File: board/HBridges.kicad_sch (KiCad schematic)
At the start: 66 parts, among them Q1 NMOS, Q2 NMOS, Q3 NMOS, Q4 NMOS, Q7 NMOS, Q8 NMOS

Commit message: Adjusted diode footprints and grouped layout components
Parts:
- C2, C24, C8: footprint BoCoFootprintLibrary:U1-Z_NCH -> Capacitor_THT:CP_Radial_D12.5mm_P5.00mm
- CR1, CR2, CR3, CR4, CR7, CR8: footprint BoCoFootprintLibrary:DO-35_STM -> Diode_THT:D_DO-35_SOD27_P3.81mm_Vertical_KathodeUp
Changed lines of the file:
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@@
 			)
 		)
-		(property "Footprint" "BoCoFootprintLibrary:U1-Z_NCH"
+		(property "Footprint" "Capacitor_THT:CP_Radial_D12.5mm_P5.00mm"
 			(at 128.27 31.75 0)
 			(effects
@@
 			)
 		)
-		(property "Footprint" "BoCoFootprintLibrary:DO-35_STM"
+		(property "Footprint" "Diode_THT:D_DO-35_SOD27_P3.81mm_Vertical_KathodeUp"
 			(at 158.75 86.36 0)
 			(effects
@@
 			)
 		)
-		(property "Footprint" "BoCoFootprintLibrary:DO-35_STM"
+		(property "Footprint" "Diode_THT:D_DO-35_SOD27_P3.81mm_Vertical_KathodeUp"
 			(at 158.75 41.91 0)
 			(effects
@@
 			)
 		)
-		(property "Footprint" "BoCoFootprintLibrary:DO-35_STM"
+		(property "Footprint" "Diode_THT:D_DO-35_SOD27_P3.81mm_Vertical_KathodeUp"
 			(at 93.98 86.36 0)
 			(effects
@@
 			)
 		)
-		(property "Footprint" "BoCoFootprintLibrary:U1-Z_NCH"
+		(property "Footprint" "Capacitor_THT:CP_Radial_D12.5mm_P5.00mm"
 			(at 63.5 31.75 0)
 			(effects
@@
 			)
 		)
-		(property "Footprint" "BoCoFootprintLibrary:DO-35_STM"
+		(property "Footprint" "Diode_THT:D_DO-35_SOD27_P3.81mm_Vertical_KathodeUp"
 			(at 93.98 41.91 0)
 			(effects
@@
 			)
 		)
-		(property "Footprint" "BoCoFootprintLibrary:DO-35_STM"
+		(property "Footprint" "Diode_THT:D_DO-35_SOD27_P3.81mm_Vertical_KathodeUp"
 			(at 29.21 41.91 0)
 			(effects
@@
 			)
 		)
-		(property "Footprint" "BoCoFootprintLibrary:DO-35_STM"
+		(property "Footprint" "Diode_THT:D_DO-35_SOD27_P3.81mm_Vertical_KathodeUp"
 			(at 29.21 86.36 0)
 			(effects
@@
 			)
 		)
-		(property "Footprint" "BoCoFootprintLibrary:U1-Z_NCH"
+		(property "Footprint" "Capacitor_THT:CP_Radial_D12.5mm_P5.00mm"
 			(at 193.04 31.75 0)
 			(effects

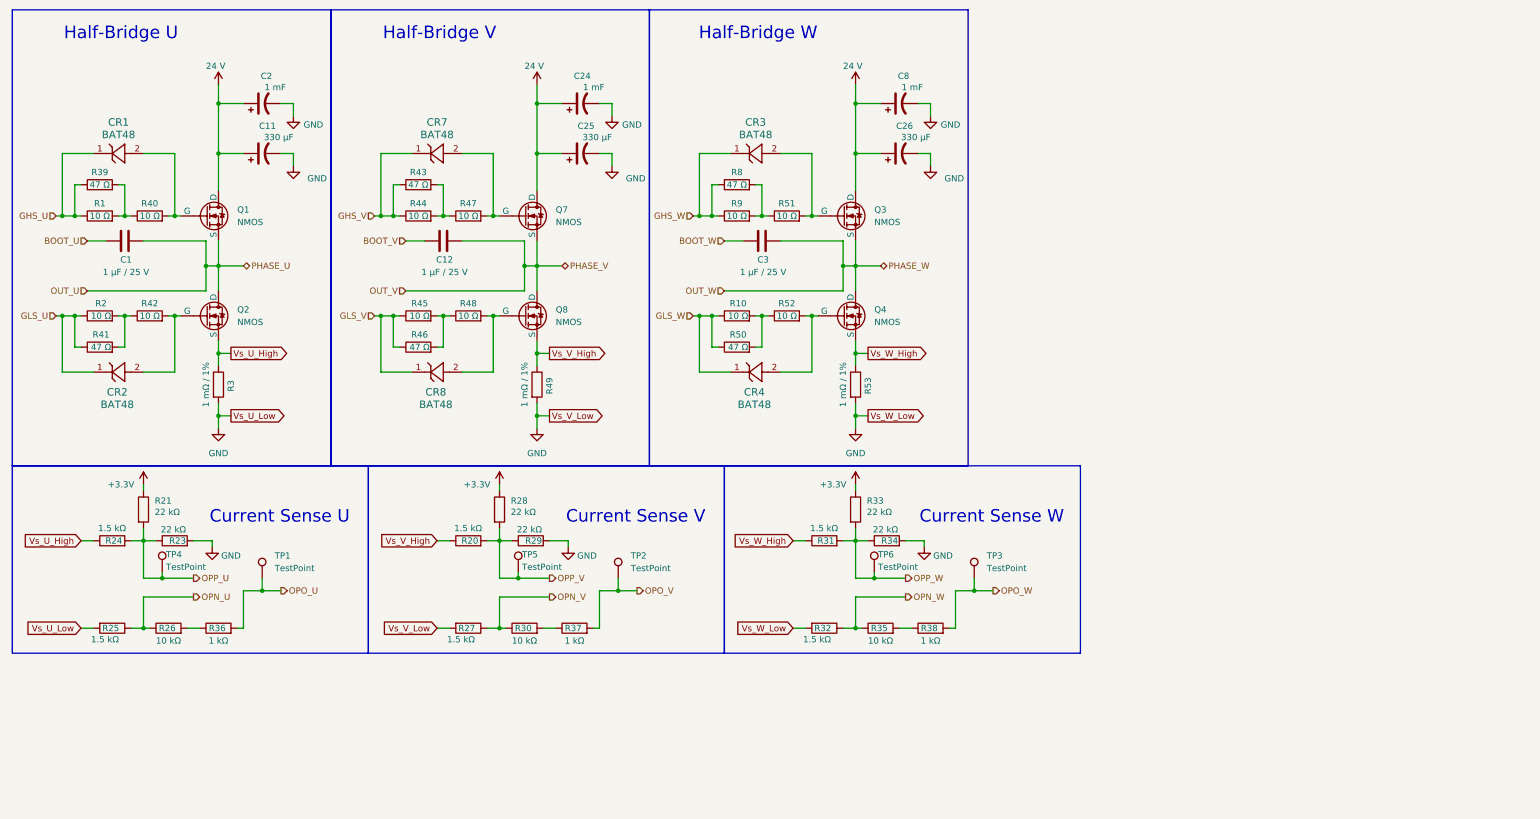
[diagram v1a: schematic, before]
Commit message: Placed some basic planes in the layout and swapped mosfet symbols to match layout footprints.
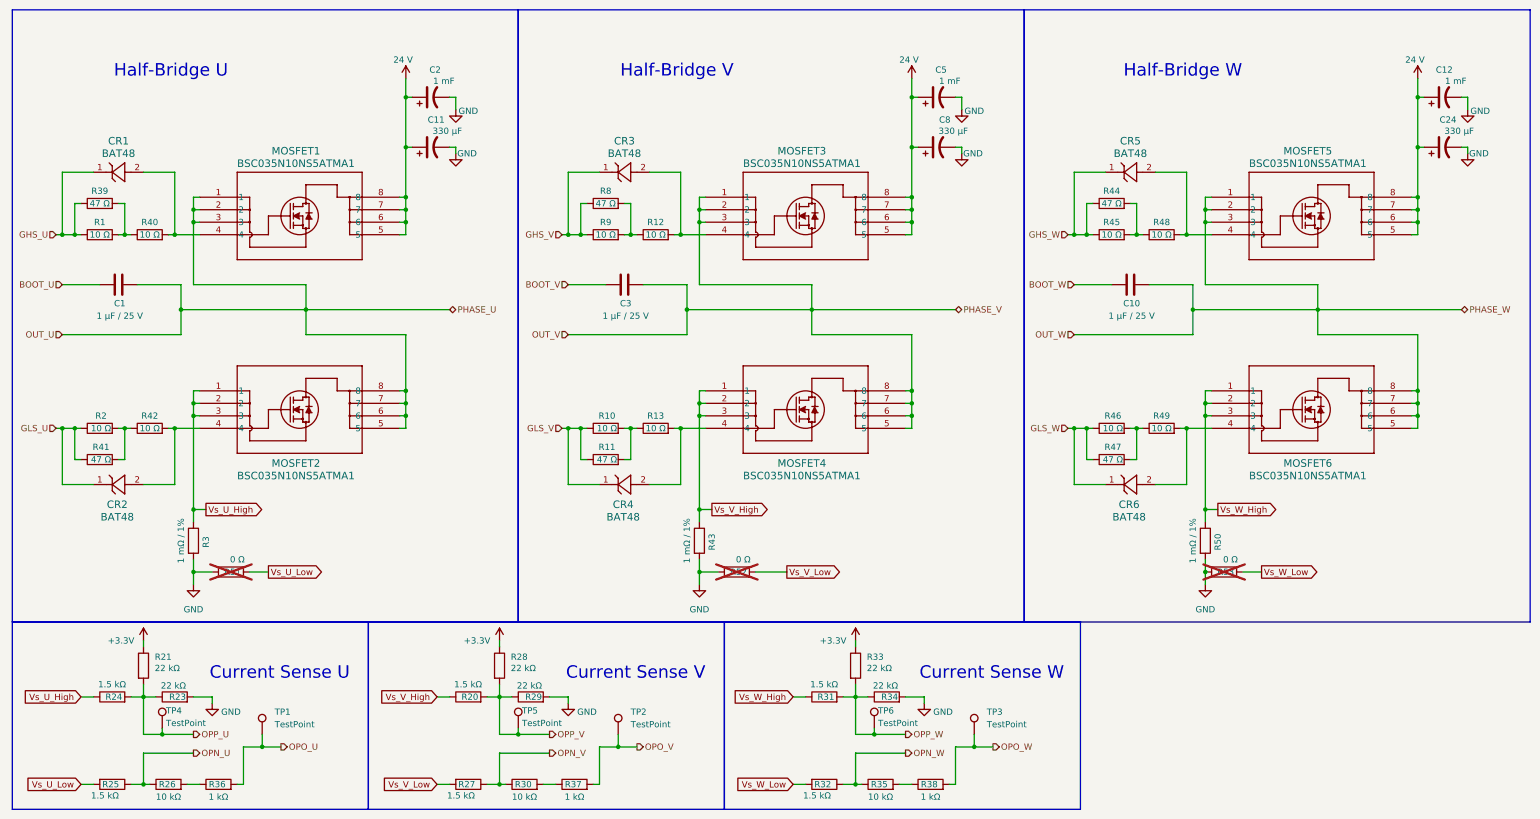
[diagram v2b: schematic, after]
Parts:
- removed C12: 1 µF / 25 V, Capacitor_SMD:C_0603_1608Metric_Pad1.08x0.95mm_HandSolder, symbol Device:C
- removed C25, C26: 330 μF, BoCoFootprintLibrary:CAP_PAN_EEE_H13_PAN, symbol Device:C_Polarized_US
- removed CR7, CR8: BAT48, Diode_THT:D_DO-35_SOD27_P3.81mm_Vertical_KathodeUp, symbol BAT48:BAT48
- removed Q1, Q2, Q3, Q4, Q7, Q8: NMOS, BoCoFootprintLibrary:PG-TDSON-8_INF, symbol Simulation_SPICE:NMOS
- added C10: 1 µF / 25 V, Capacitor_SMD:C_0603_1608Metric_Pad1.08x0.95mm_HandSolder, symbol Device:C
- added C12, C5: 1 mF, Capacitor_THT:CP_Radial_D12.5mm_P5.00mm, symbol Device:C_Polarized_US
- added CR5, CR6: BAT48, Diode_THT:D_DO-35_SOD27_P3.81mm_Vertical_KathodeUp, symbol BAT48:BAT48
- added MOSFET1, MOSFET2, MOSFET3, MOSFET4, MOSFET5, MOSFET6: BSC035N10NS5ATMA1, PG-TDSON-8_INF, symbol BoCoSymbolLibrary:BSC035N10NS5ATMA1
- added R11: 47 Ω, Resistor_SMD:R_0603_1608Metric_Pad0.98x0.95mm_HandSolder, symbol Device:R
- added R12, R13: 10 Ω, Resistor_SMD:R_0603_1608Metric_Pad0.98x0.95mm_HandSolder, symbol Device:R
- C24, C8: value 1 mF -> 330 μF; footprint Capacitor_THT:CP_Radial_D12.5mm_P5.00mm -> BoCoFootprintLibrary:CAP_PAN_EEE_H13_PAN
- R43, R50: value 47 Ω -> 1 mΩ / 1%
- R44, R47: value 10 Ω -> 47 Ω
- R46: value 47 Ω -> 10 Ω
- R49: value 1 mΩ / 1% -> 10 Ω
- R51, R52: value 10 Ω -> 0 Ω; now not fitted
- R53: value 1 mΩ / 1% -> 0 Ω; now not fitted
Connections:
- net 24 V: now also C12.1, C5.1, MOSFET1.5, MOSFET1.6, MOSFET1.7, MOSFET1.8, MOSFET3.5, MOSFET3.6, MOSFET3.7, MOSFET3.8, MOSFET5.5, MOSFET5.6, MOSFET5.7, MOSFET5.8
- net BOOT_V: now also C3.1
- net BOOT_W: now also C10.1; no longer C3.1
- net GHS_V: now also CR3.1, R8.1, R9.1; no longer R43.1, R44.1
- net GHS_W: now also R44.1, R45.1, CR5.1; no longer CR3.1, R8.1, R9.1
- net GLS_V: now also CR4.1, R10.1, R11.1; no longer R45.1, R46.1
- net GLS_W: now also R46.1, R47.1, CR6.1; no longer CR4.1, R10.1, R50.1
- net GND: now also R43.2, R50.2, R51.1, R52.1, R53.1, C12.2, C5.2; no longer R25.2, R27.2, R32.2, R49.2, R53.2
- net OUT_U: now also MOSFET1.1, MOSFET1.2, MOSFET1.3, MOSFET2.5, MOSFET2.6, MOSFET2.7, MOSFET2.8
- net OUT_V: now also C3.2, MOSFET3.1, MOSFET3.2, MOSFET3.3, MOSFET4.5, MOSFET4.6, MOSFET4.7, MOSFET4.8
- net OUT_W: now also C10.2, MOSFET5.1, MOSFET5.2, MOSFET5.3, MOSFET6.5, MOSFET6.6, MOSFET6.7, MOSFET6.8; no longer C3.2
- net Vs_U_High: now also MOSFET2.1, MOSFET2.2, MOSFET2.3
- net Vs_V_High: now also R43.1, MOSFET4.1, MOSFET4.2, MOSFET4.3; no longer R49.1
- net Vs_W_High: now also R50.1, MOSFET6.1, MOSFET6.2, MOSFET6.3; no longer R53.1
- net at CR3.2: now also MOSFET3.4, R12.2; no longer R51.2
- net at CR4.2: now also MOSFET4.4, R13.2; no longer R52.2
- net at R47.2: now also R46.2, R49.1
- net at R48.2: now also CR5.2, MOSFET5.4
- net at R45.2, R48.1: now also R44.2; no longer R46.2
- net at CR1.2, R40.2: now also MOSFET1.4
- net at R8.2, R9.2: now also R12.1; no longer R51.1
- net at CR2.2, R42.2: now also MOSFET2.4
- new net: R10.2, R11.2, R13.1
- new net: CR6.2, MOSFET6.4, R49.2
- new net Vs_U_Low: R25.2, R51.2
- new net Vs_V_Low: R27.2, R52.2
- new net Vs_W_Low: R32.2, R53.2
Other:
- moved on the sheet: C1, C11, C2, CR1, CR2, R1, R2, R20, R21, R23, R24, R25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

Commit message: Updated footprints to fix issues found in board review.
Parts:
- removed C11, C24, C8: 330 μF, BoCoFootprintLibrary:CAP_PAN_EEE_H13_PAN, symbol Device:C_Polarized_US
- removed C12, C2, C5: 1 mF, Capacitor_THT:CP_Radial_D12.5mm_P5.00mm, symbol Device:C_Polarized_US
- removed TP1, TP2, TP3, TP4, TP5, TP6: TestPoint, TestPoint:TestPoint_Pad_D4.0mm, symbol Connector:TestPoint
- MOSFET1, MOSFET2, MOSFET3, MOSFET4, MOSFET5, MOSFET6: footprint PG-TDSON-8_INF -> BoCoFootprintLibrary:PG-TDSON-8_INF

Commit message: Made layout adjustments according to board review.
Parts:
- removed CR1, CR2, CR3, CR4, CR5, CR6: BAT48, Diode_THT:D_DO-35_SOD27_P3.81mm_Vertical_KathodeUp, symbol BAT48:BAT48
- removed R51, R52, R53: 0 Ω, Resistor_SMD:R_0603_1608Metric_Pad0.98x0.95mm_HandSolder, symbol Device:R
- added D2, D4, D5, D6, D7, D8: D_Schottky, Diode_SMD:D_SOD-123, symbol Device:D_Schottky
- added NT1, NT2, NT3: NetTie_2, NetTie:NetTie-2_SMD_Pad0.5mm, symbol Device:NetTie_2
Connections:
- net GHS_U: now also D2.1 (K)
- net GHS_V: now also D5.1 (K)
- net GHS_W: now also D6.1 (K)
- net GLS_U: now also D4.1 (K)
- net GLS_V: now also D7.1 (K)
- net GLS_W: now also D8.1 (K)
- net GND: now also NT1.1, NT2.1, NT3.1
- net Vs_U_Low: now also NT3.2
- net Vs_V_Low: now also NT2.2
- net Vs_W_Low: now also NT1.2
- net at MOSFET3.4, R12.2: now also D5.2 (A)
- net at MOSFET1.4, R40.2: now also D2.2 (A)
- net at MOSFET4.4, R13.2: now also D7.2 (A)
- net at MOSFET2.4, R42.2: now also D4.2 (A)
- net at MOSFET5.4, R48.2: now also D6.2 (A)
- net at MOSFET6.4, R49.2: now also D8.2 (A)

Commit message: Fixed footprint and symbol for FETs
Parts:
- MOSFET1, MOSFET2, MOSFET3, MOSFET4, MOSFET5, MOSFET6: footprint BoCoFootprintLibrary:PG-TDSON-8_INF -> PG-TDSON-8_INF
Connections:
- net 24 V: no longer MOSFET1.6, MOSFET1.7, MOSFET1.8, MOSFET3.6, MOSFET3.7, MOSFET3.8, MOSFET5.6, MOSFET5.7, MOSFET5.8
- net OUT_U: no longer MOSFET2.6, MOSFET2.7, MOSFET2.8
- net OUT_V: no longer MOSFET4.6, MOSFET4.7, MOSFET4.8
- net OUT_W: no longer MOSFET6.6, MOSFET6.7, MOSFET6.8
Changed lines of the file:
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@@
 			)
 		)
-		(property "Footprint" "BoCoFootprintLibrary:PG-TDSON-8_INF"
+		(property "Footprint" "PG-TDSON-8_INF"
 			(at 153.67 50.8 0)
 			(effects
@@
 			)
 		)
-		(pin "7"
-		)
 		(pin "5"
 		)
@@
 		(pin "3"
 		)
-		(pin "8"
-		)
 		(pin "4"
 		)
 		(pin "1"
 		)
-		(pin "6"
-		)
 		(instances
 			(project "BrushlessMocoBoard"
@@
 			)
 		)
-		(property "Footprint" "BoCoFootprintLibrary:PG-TDSON-8_INF"
+		(property "Footprint" "PG-TDSON-8_INF"
 			(at 50.8 50.8 0)
 			(effects
@@
 			)
 		)
-		(pin "7"
-		)
 		(pin "5"
 		)
@@
 		(pin "3"
 		)
-		(pin "8"
-		)
 		(pin "4"
 		)
 		(pin "1"
 		)
-		(pin "6"
-		)
 		(instances
 			(project ""
@@
 			)
 		)
-		(property "Footprint" "BoCoFootprintLibrary:PG-TDSON-8_INF"
+		(property "Footprint" "PG-TDSON-8_INF"
 			(at 50.8 90.17 0)
 			(effects
@@
 			)
 		)
-		(pin "7"
-		)
 		(pin "5"
 		)
@@
 		(pin "3"
 		)
-		(pin "8"
-		)
 		(pin "4"
 		)
 		(pin "1"
 		)
-		(pin "6"
-		)
 		(instances
 			(project "BrushlessMocoBoard"
@@
 			)
 		)
-		(property "Footprint" "BoCoFootprintLibrary:PG-TDSON-8_INF"
+		(property "Footprint" "PG-TDSON-8_INF"
 			(at 153.67 90.17 0)
 			(effects
@@
 			)
 		)
-		(pin "7"
-		)
 		(pin "5"
 		)
@@
 		(pin "3"
 		)
-		(pin "8"
-		)
 		(pin "4"
 		)
 		(pin "1"
 		)
-		(pin "6"
-		)
 		(instances
 			(project "BrushlessMocoBoard"
@@
 			)
 		)
-		(property "Footprint" "BoCoFootprintLibrary:PG-TDSON-8_INF"
+		(property "Footprint" "PG-TDSON-8_INF"
 			(at 256.54 90.17 0)
 			(effects
@@
 			)
 		)
-		(pin "7"
-		)
 		(pin "5"
 		)
@@
 		(pin "3"
 		)
-		(pin "8"
-		)
 		(pin "4"
 		)
 		(pin "1"
 		)
-		(pin "6"
-		)
 		(instances
 			(project "BrushlessMocoBoard"
@@
 			)
 		)
-		(property "Footprint" "BoCoFootprintLibrary:PG-TDSON-8_INF"
+		(property "Footprint" "PG-TDSON-8_INF"
 			(at 256.54 50.8 0)
 			(effects
@@
 			)
 		)
-		(pin "7"
-		)
 		(pin "5"
 		)
@@
 		(pin "3"
 		)
-		(pin "8"
-		)
 		(pin "4"
 		)
 		(pin "1"
 		)
-		(pin "6"
-		)
 		(instances

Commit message: Tentatively finished rev1.
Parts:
- MOSFET1, MOSFET2, MOSFET3, MOSFET4, MOSFET5, MOSFET6: footprint PG-TDSON-8_INF -> BoCoFootprintLibrary:PG-TDSON-8_INF
- R3, R43, R50: footprint Resistor_SMD:R_0603_1608Metric_Pad0.98x0.95mm_HandSolder -> Resistor_SMD:R_1206_3216Metric_Pad1.30x1.75mm_HandSolder
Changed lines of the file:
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@@
 			)
 		)
-		(property "Footprint" "PG-TDSON-8_INF"
+		(property "Footprint" "BoCoFootprintLibrary:PG-TDSON-8_INF"
 			(at 153.67 50.8 0)
 			(effects
@@
 			)
 		)
-		(property "Footprint" "Resistor_SMD:R_0603_1608Metric_Pad0.98x0.95mm_HandSolder"
+		(property "Footprint" "Resistor_SMD:R_1206_3216Metric_Pad1.30x1.75mm_HandSolder"
 			(at 253.492 120.65 90)
 			(effects
@@
 			)
 		)
-		(property "Footprint" "PG-TDSON-8_INF"
+		(property "Footprint" "BoCoFootprintLibrary:PG-TDSON-8_INF"
 			(at 50.8 50.8 0)
 			(effects
@@
 			)
 		)
-		(property "Footprint" "PG-TDSON-8_INF"
+		(property "Footprint" "BoCoFootprintLibrary:PG-TDSON-8_INF"
 			(at 50.8 90.17 0)
 			(effects
@@
 			)
 		)
-		(property "Footprint" "PG-TDSON-8_INF"
+		(property "Footprint" "BoCoFootprintLibrary:PG-TDSON-8_INF"
 			(at 153.67 90.17 0)
 			(effects
@@
 			)
 		)
-		(property "Footprint" "Resistor_SMD:R_0603_1608Metric_Pad0.98x0.95mm_HandSolder"
+		(property "Footprint" "Resistor_SMD:R_1206_3216Metric_Pad1.30x1.75mm_HandSolder"
 			(at 47.752 120.65 90)
 			(effects
@@
 			)
 		)
-		(property "Footprint" "PG-TDSON-8_INF"
+		(property "Footprint" "BoCoFootprintLibrary:PG-TDSON-8_INF"
 			(at 256.54 90.17 0)
 			(effects
@@
 			)
 		)
-		(property "Footprint" "Resistor_SMD:R_0603_1608Metric_Pad0.98x0.95mm_HandSolder"
+		(property "Footprint" "Resistor_SMD:R_1206_3216Metric_Pad1.30x1.75mm_HandSolder"
 			(at 150.622 120.65 90)
 			(effects
@@
 			)
 		)
-		(property "Footprint" "PG-TDSON-8_INF"
+		(property "Footprint" "BoCoFootprintLibrary:PG-TDSON-8_INF"
 			(at 256.54 50.8 0)
 			(effects

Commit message: Fixed many issues found in Rev1 review prior to order
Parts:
- renumbered MOSFET1 to Q1, MOSFET2 to Q2, MOSFET3 to Q3, MOSFET4 to Q4, MOSFET5 to Q5, MOSFET6 to Q6
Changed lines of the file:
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@@
 		(on_board yes)
 		(dnp no)
-		(property "Reference" "MOSFET3"
+		(property "Reference" "Q3"
 			(at 173.228 41.402 0)
 			(effects
@@
 			(project "BrushlessMocoBoard"
 				(path "/1ef8bc88-f0df-4a97-862b-c4b9ec3b4ed0/9ba7f673-fd83-4be7-b86a-03ddf33e37d2"
-					(reference "MOSFET3")
+					(reference "Q3")
 					(unit 1)
 				)
@@
 		(on_board yes)
 		(dnp no)
-		(property "Reference" "MOSFET1"
+		(property "Reference" "Q1"
 			(at 70.358 41.402 0)
 			(effects
@@
 			(project ""
 				(path "/1ef8bc88-f0df-4a97-862b-c4b9ec3b4ed0/9ba7f673-fd83-4be7-b86a-03ddf33e37d2"
-					(reference "MOSFET1")
+					(reference "Q1")
 					(unit 1)
 				)
@@
 		(on_board yes)
 		(dnp no)
-		(property "Reference" "MOSFET2"
+		(property "Reference" "Q2"
 			(at 70.358 104.902 0)
 			(effects
@@
 			(project "BrushlessMocoBoard"
 				(path "/1ef8bc88-f0df-4a97-862b-c4b9ec3b4ed0/9ba7f673-fd83-4be7-b86a-03ddf33e37d2"
-					(reference "MOSFET2")
+					(reference "Q2")
 					(unit 1)
 				)
@@
 		(on_board yes)
 		(dnp no)
-		(property "Reference" "MOSFET4"
+		(property "Reference" "Q4"
 			(at 173.228 104.902 0)
 			(effects
@@
 			(project "BrushlessMocoBoard"
 				(path "/1ef8bc88-f0df-4a97-862b-c4b9ec3b4ed0/9ba7f673-fd83-4be7-b86a-03ddf33e37d2"
-					(reference "MOSFET4")
+					(reference "Q4")
 					(unit 1)
 				)
@@
 		(on_board yes)
 		(dnp no)
-		(property "Reference" "MOSFET6"
+		(property "Reference" "Q6"
 			(at 276.098 104.902 0)
 			(effects
@@
 			(project "BrushlessMocoBoard"
 				(path "/1ef8bc88-f0df-4a97-862b-c4b9ec3b4ed0/9ba7f673-fd83-4be7-b86a-03ddf33e37d2"
-					(reference "MOSFET6")
+					(reference "Q6")
 					(unit 1)
 				)
@@
 		(on_board yes)
 		(dnp no)
-		(property "Reference" "MOSFET5"
+		(property "Reference" "Q5"
 			(at 276.098 41.402 0)
 			(effects
@@
 			(project "BrushlessMocoBoard"
 				(path "/1ef8bc88-f0df-4a97-862b-c4b9ec3b4ed0/9ba7f673-fd83-4be7-b86a-03ddf33e37d2"
-					(reference "MOSFET5")
+					(reference "Q5")
 					(unit 1)
 				)

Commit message: Added footprints to board library
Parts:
- Q1, Q2, Q3, Q4, Q5, Q6: footprint BoCoFootprintLibrary:PG-TDSON-8_INF -> BrushlessMocoBoard:PG-TDSON-8_INF
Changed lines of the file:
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@@
 			)
 		)
-		(property "Footprint" "BoCoFootprintLibrary:PG-TDSON-8_INF"
+		(property "Footprint" "BrushlessMocoBoard:PG-TDSON-8_INF"
 			(at 153.67 50.8 0)
 			(effects
@@
 			)
 		)
-		(property "Footprint" "BoCoFootprintLibrary:PG-TDSON-8_INF"
+		(property "Footprint" "BrushlessMocoBoard:PG-TDSON-8_INF"
 			(at 50.8 50.8 0)
 			(effects
@@
 			)
 		)
-		(property "Footprint" "BoCoFootprintLibrary:PG-TDSON-8_INF"
+		(property "Footprint" "BrushlessMocoBoard:PG-TDSON-8_INF"
 			(at 50.8 90.17 0)
 			(effects
@@
 			)
 		)
-		(property "Footprint" "BoCoFootprintLibrary:PG-TDSON-8_INF"
+		(property "Footprint" "BrushlessMocoBoard:PG-TDSON-8_INF"
 			(at 153.67 90.17 0)
 			(effects
@@
 			)
 		)
-		(property "Footprint" "BoCoFootprintLibrary:PG-TDSON-8_INF"
+		(property "Footprint" "BrushlessMocoBoard:PG-TDSON-8_INF"
 			(at 256.54 90.17 0)
 			(effects
@@
 			)
 		)
-		(property "Footprint" "BoCoFootprintLibrary:PG-TDSON-8_INF"
+		(property "Footprint" "BrushlessMocoBoard:PG-TDSON-8_INF"
 			(at 256.54 50.8 0)
 			(effects
